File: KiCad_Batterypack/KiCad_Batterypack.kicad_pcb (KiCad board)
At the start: 2 copper layers, 86 x 42 mm, 7 parts, among them J1 Screw_Terminal_01x02

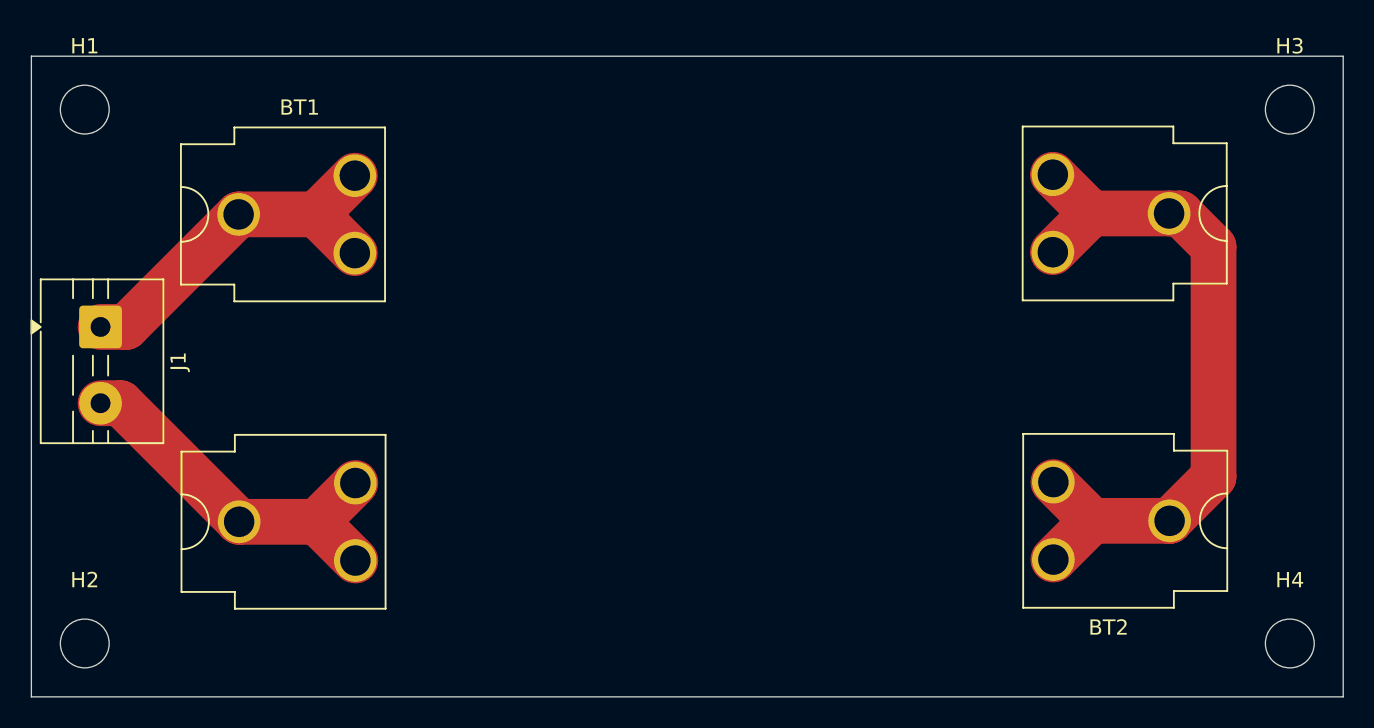
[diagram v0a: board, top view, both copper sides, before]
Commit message: Added plane
Added grounded plane on front and back to reduce machining
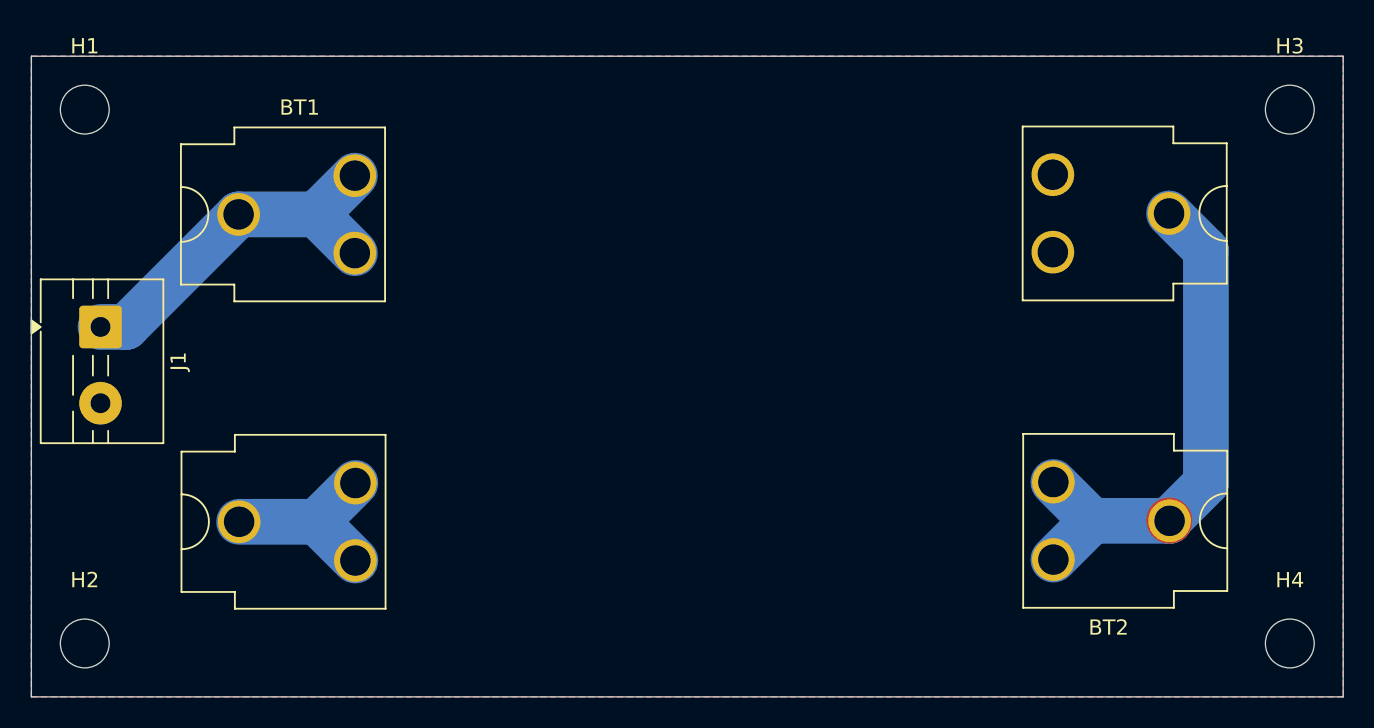
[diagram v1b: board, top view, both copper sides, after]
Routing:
- net Net-(BT1--): track 47.6 -> 34.5 mm
- net GND: track 24.6 -> 12.3 mm
- added copper zone on B.Cu, net GND
- added copper zone on F.Cu, net GND
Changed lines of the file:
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@@
-	)
-	(segment
-		(start 97.5 47.58)
-		(end 94.62 50.46)
-		(width 3)
-		(layer "F.Cu")
-		(net 1)
-	)
-	(segment
-		(start 89.54 50.46)
-		(end 87 53)
-		(width 3)
-		(layer "F.Cu")
-		(net 1)
 	)
 	(segment
@@
 	)
 	(segment
-		(start 94.585445 30.308343)
-		(end 95.308343 30.308343)
+		(start 94.62 50.46)
+		(end 94.62 50.38)
 		(width 3)
-		(layer "F.Cu")
+		(layer "B.Cu")
+		(net 1)
+	)
+	(segment
+		(start 94.62 50.46)
+		(end 89.54 50.46)
+		(width 3)
+		(layer "B.Cu")
+		(net 1)
+	)
+	(segment
+		(start 94.62 50.38)
+		(end 97 48)
+		(width 3)
+		(layer "B.Cu")
 		(net 1)
 	)
@@
 		(end 87 47.92)
 		(width 3)
-		(layer "F.Cu")
+		(layer "B.Cu")
 		(net 1)
 	)
 	(segment
-		(start 95.308343 30.308343)
-		(end 97.5 32.5)
+		(start 97 48)
+		(end 97 32.722898)
 		(width 3)
-		(layer "F.Cu")
+		(layer "B.Cu")
 		(net 1)
 	)
 	(segment
-		(start 94.585445 30.308343)
-		(end 89.505445 30.308343)
+		(start 97 32.722898)
+		(end 94.585445 30.308343)
 		(width 3)
-		(layer "F.Cu")
+		(layer "B.Cu")
 		(net 1)
 	)
 	(segment
-		(start 89.505445 30.308343)
-		(end 86.965445 27.768343)
+		(start 89.54 50.46)
+		(end 87 53)
 		(width 3)
-		(layer "F.Cu")
-		(net 1)
-	)
-	(segment
-		(start 97.5 32.5)
-		(end 97.5 47.58)
-		(width 3)
-		(layer "F.Cu")
-		(net 1)
-	)
-	(segment
-		(start 94.62 50.46)
-		(end 89.54 50.46)
-		(width 3)
-		(layer "F.Cu")
-		(net 1)
-	)
-	(segment
-		(start 89.505445 30.308343)
-		(end 86.965445 32.848343)
-		(width 3)
-		(layer "F.Cu")
+		(layer "B.Cu")
 		(net 1)
 	)
@@
 		(end 26.206388 37.75)
 		(width 3)
-		(layer "F.Cu")
+		(layer "B.Cu")
+		(net 2)
+	)
+	(segment
+		(start 38.665445 30.370943)
+		(end 41.205445 32.910943)
+		(width 3)
+		(layer "B.Cu")
 		(net 2)
 	)
@@
 		(end 41.205445 27.830943)
 		(width 3)
-		(layer "F.Cu")
+		(layer "B.Cu")
+		(net 2)
+	)
+	(segment
+		(start 26.206388 37.75)
+		(end 33.585445 30.370943)
+		(width 3)
+		(layer "B.Cu")
 		(net 2)
 	)
@@
 		(end 38.665445 30.370943)
 		(width 3)
-		(layer "F.Cu")
+		(layer "B.Cu")
 		(net 2)
-	)
-	(segment
-		(start 38.665445 30.370943)
-		(end 41.205445 32.910943)
-		(width 3)
-		(layer "F.Cu")
-		(net 2)
-	)
-	(segment
-		(start 26.206388 37.75)
-		(end 33.585445 30.370943)
-		(width 3)
-		(layer "F.Cu")
-		(net 2)
-	)
-	(segment
-		(start 24.5325 42.75)
-		(end 25.8474 42.75)
-		(width 3)
-		(layer "F.Cu")
-		(net 3)
 	)
 	(segment
@@
 		(end 41.24 53.0626)
 		(width 3)
-		(layer "F.Cu")
+		(layer "B.Cu")
+		(net 3)
+	)
+	(segment
+		(start 33.62 50.5226)
+		(end 38.7 50.5226)
+		(width 3)
+		(layer "B.Cu")
 		(net 3)
 	)
@@
 		(end 41.24 47.9826)
 		(width 3)
-		(layer "F.Cu")
+		(layer "B.Cu")
 		(net 3)
 	)
-	(segment
-		(start 33.62 50.5226)
-		(end 38.7 50.5226)
-		(width 3)
-		(layer "F.Cu")
+	(zone
 		(net 3)
-	)
-	(segment
-		(start 25.8474 42.75)
-		(end 33.62 50.5226)
-		(width 3)
-		(layer "F.Cu")
-		(net 3)
+		(net_name "GND")
+		(layers "F.Cu" "B.Cu")
+		(name "GND_Plane")
+		(hatch edge 0.5)
+		(connect_pads
+			(clearance 0.5)
+		)
+		(min_thickness 0.4)
+		(filled_areas_thickness no)
+		(fill yes
+			(thermal_gap 0.5)
+			(thermal_bridge_width 0.6)
+			(smoothing fillet)
+			(radius 0.2)
+		)
+		(polygon
+			(pts
+				(xy 20 20) (xy 106 20) (xy 106 62) (xy 20 62)
+			)
+		)
 	)
 	(embedded_fonts no)
